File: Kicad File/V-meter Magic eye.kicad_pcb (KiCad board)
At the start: 2 copper layers, 114.3 x 51.6 mm, 46 parts, among them J1 15V, J2 VT138 socket, J3 BF IN, Q1 BUZ11, Q2 BC547, Q3 BC547, Q4 BC547, U1 NE555P

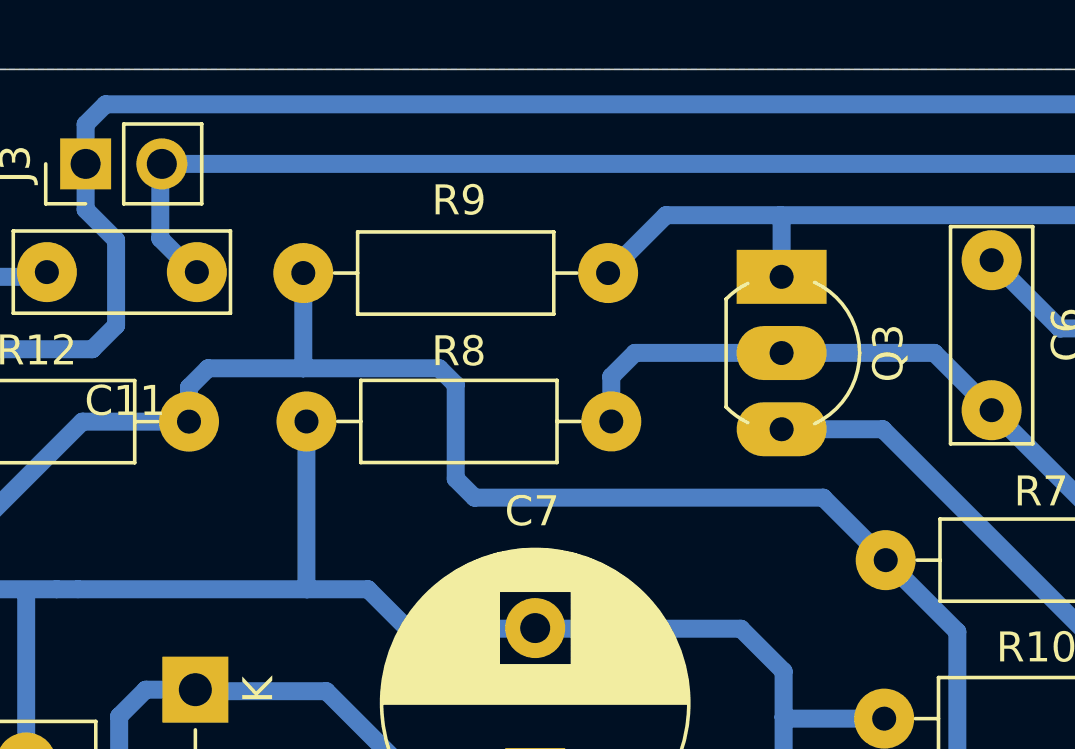
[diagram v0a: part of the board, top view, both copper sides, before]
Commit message: V 1.1
Inserito pdf dello schema elettrico PCB e montaggio componenti
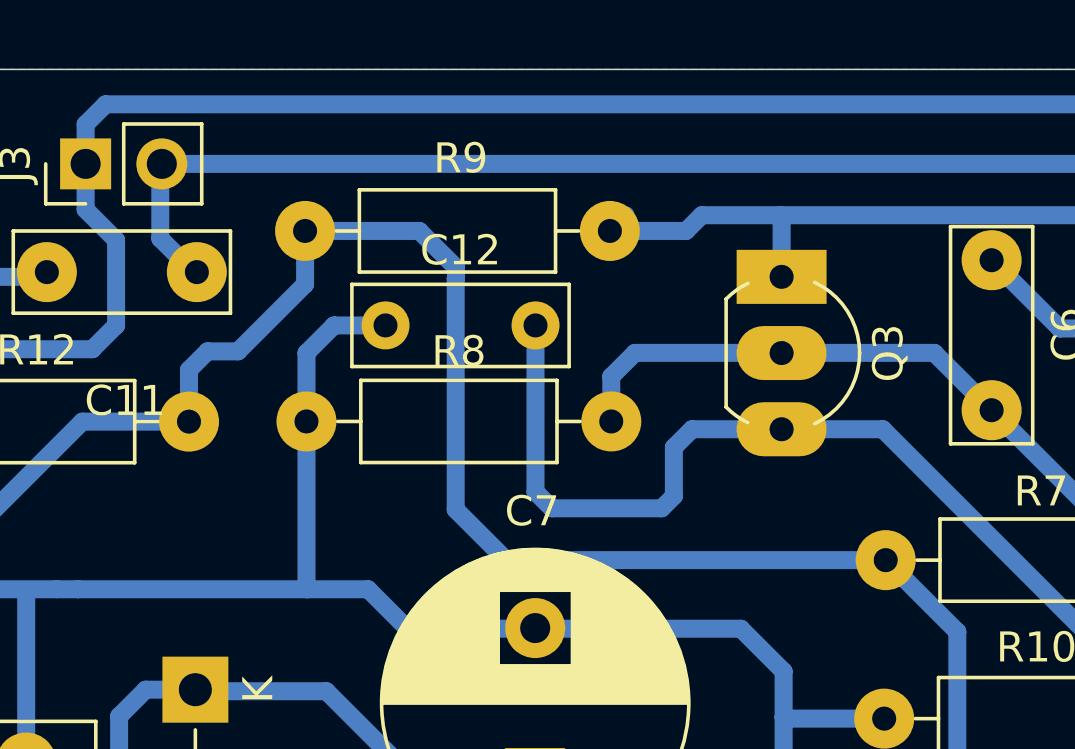
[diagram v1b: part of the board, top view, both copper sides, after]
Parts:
- added C12: 100nF, Capacitor_THT:C_Rect_L7.0mm_W2.5mm_P5.00mm, F.Cu at (138.9, 79.5)
- C1: value 470uF25v -> 470uF 25v
- C7: value 2.2uF 450v -> 10uF 450v
- D1: value 1N4007 -> RGP10M
- Q1: value BUZ11 -> IRFBG 30
- R14: value 22 1/2W -> 22 1W
- R9: value 47K -> 100K
- moved R9 1.40 mm to (146.4, 76.3)
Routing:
- net Net-(Q3-E): track 17.6 -> 33.6 mm
- net GND: track 441.4 -> 446.7 mm
- net +16V: track 281.4 -> 286.4 mm

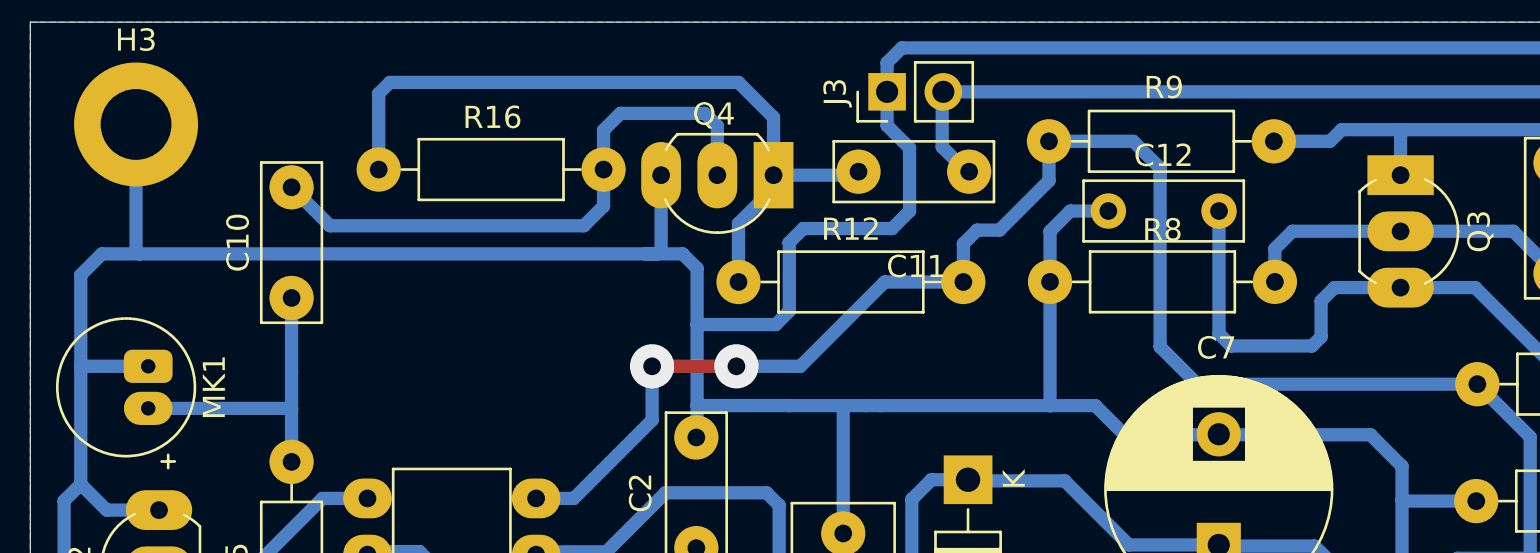
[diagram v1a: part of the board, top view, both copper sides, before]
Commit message: V1.3
inserito capacità riuzione rumore alimentazione
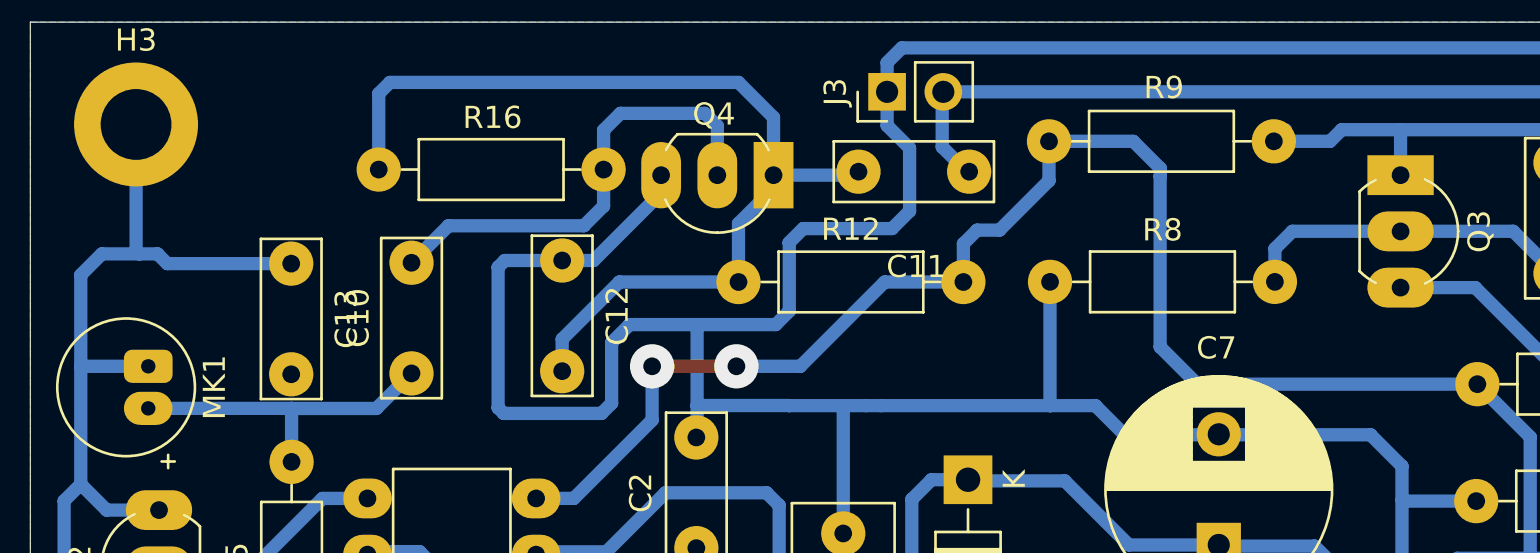
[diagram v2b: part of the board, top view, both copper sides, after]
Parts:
- added C13: 33nF, Capacitor_THT:C_Rect_L7.0mm_W2.5mm_P5.00mm, F.Cu at (102.0, 81.8)
- C1: value 470uF 25v -> 470uF25v
- moved C12 24.8 mm to (114.2, 81.7), turned to -90 degrees
- moved C10 6.40 mm to (107.4, 81.8)
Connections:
- C12 pad 2: Net-(Q3-E) -> Net-(Q4-C)
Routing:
- net Net-(Q3-E): track 33.6 -> 17.6 mm
- net Net-(Q4-C): track 34.8 -> 45.3 mm
- net Net-(Q4-B): track 26.5 -> 21.1 mm
- net GND: track 446.7 -> 444.5 mm
- net Net-(MK1-+): track 13.9 -> 15.0 mm
